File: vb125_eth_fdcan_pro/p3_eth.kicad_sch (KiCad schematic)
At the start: 28 parts, among them U2 LAN8740A, X1 50MHz

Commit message: vb125: H7 schematic WIP.
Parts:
- removed R11, R12, R13: 33R, symbol Device:R_Small
- added R11, R12, R13: 33R, Resistor_SMD:R_0402_1005Metric, symbol Device:R
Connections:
- net ETH_CRS_DV: now also R11.1
- net ETH_RXD0: now also R12.1
- net ETH_RXD1: now also R13.1
- net RXD0: now also R12.2
- net RXD1: now also R13.2
- net at R8.2, U2.15 (COL/CRS_DV/MODE2): now also R11.2
- no-connect marks 1 -> 4

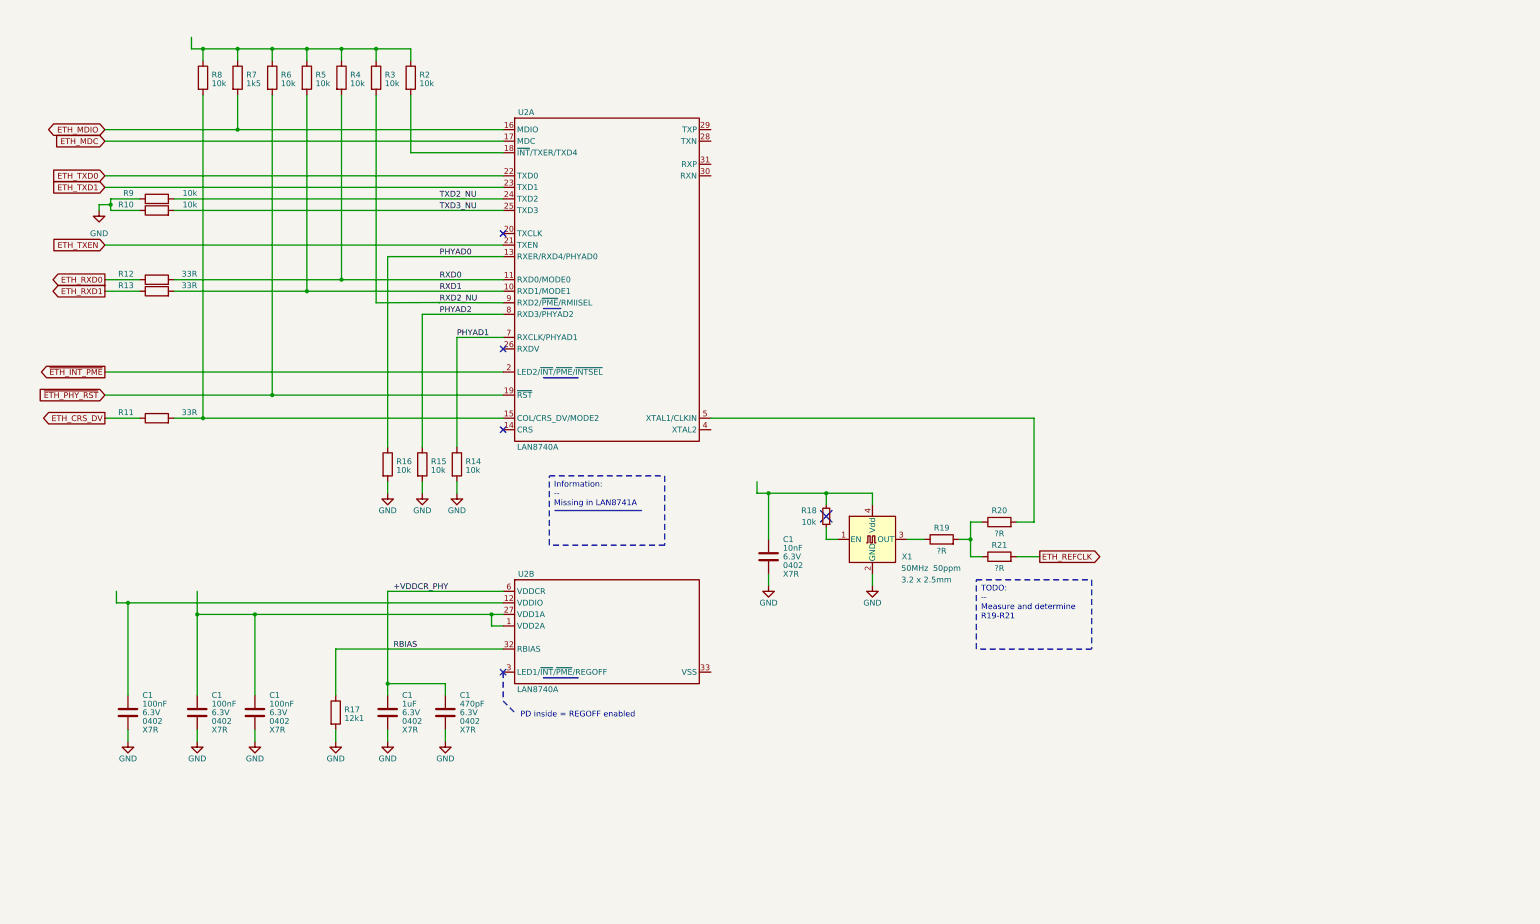
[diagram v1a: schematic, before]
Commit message: AOZ schematic. 3V3 DC-DC. Partly bus power.
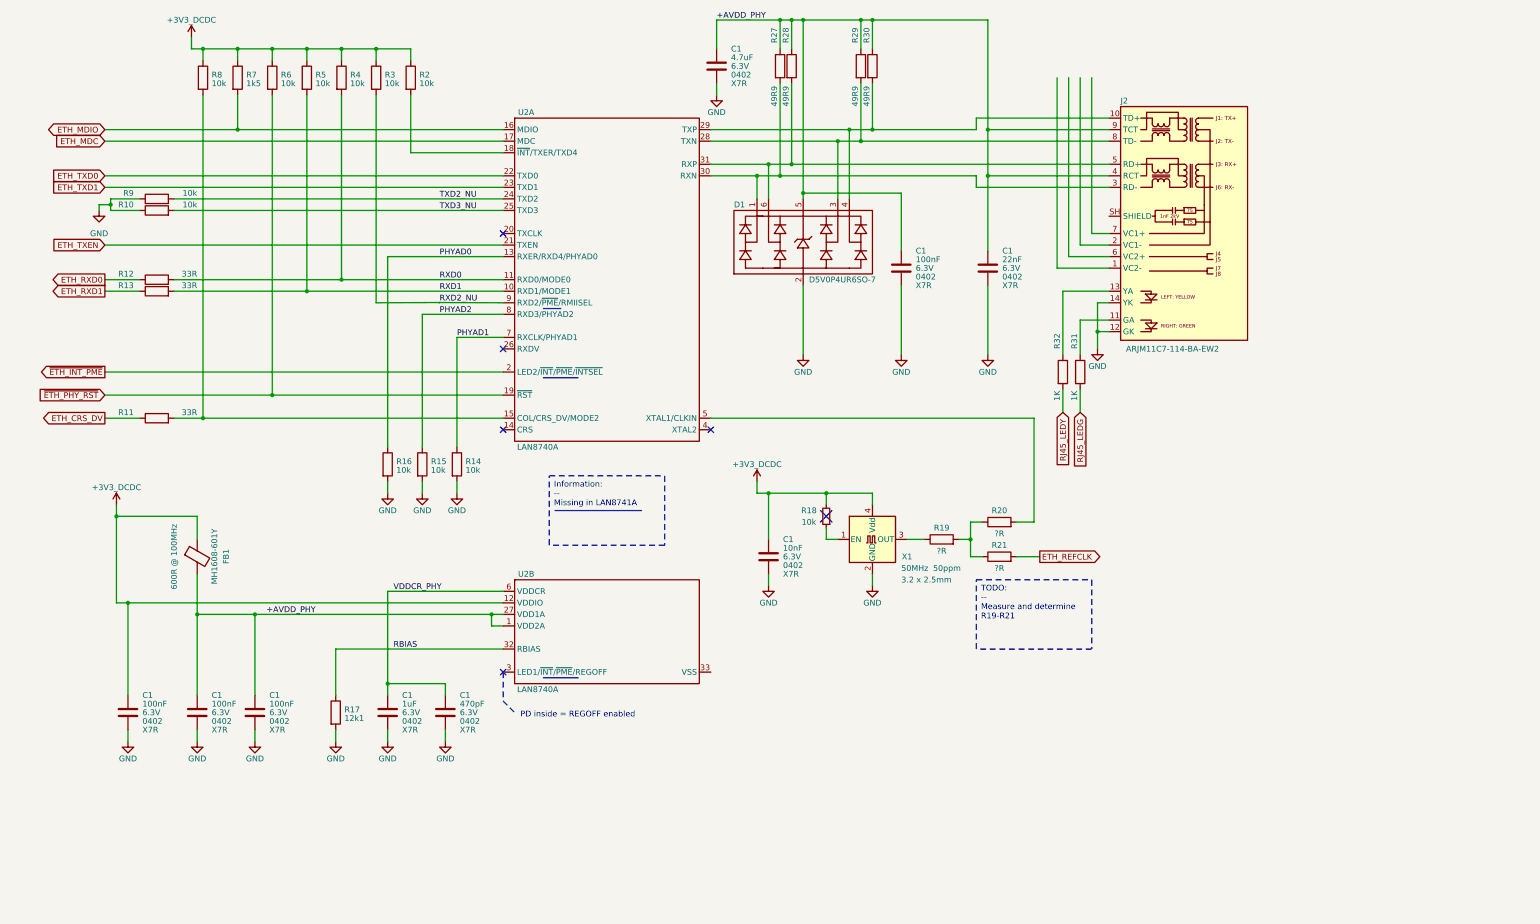
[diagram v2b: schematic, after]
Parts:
- added C1: 22nF, symbol Device:C
- added C1: 100nF, symbol Device:C
- added C1: 4.7uF, symbol Device:C
- added D1: D5V0P4UR6SO-7, vhrd_passive_tvs:D5V0P4UR6SO-7, symbol vhrd_passive_tvs:D5V0P4UR6SO-7
- added FB1: MH1608-601Y, symbol Device:FerriteBead
- added J2: ARJM11C7-114-BA-EW2, vhrd_connector_abracon:RJ45_Abracon_ARJM11_7POE_LED, symbol vhrd_connector_abracon:ARJM11C7-114-BA
- added R27, R28, R29, R30: 49R9, Resistor_SMD:R_0402_1005Metric, symbol Device:R
- added R31, R32: 1K, Resistor_SMD:R_0402_1005Metric, symbol Device:R
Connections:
- net GND: now also C1.2, C1.2, C1.2, D1.2 (VSS), J2.12 (GK), J2.14 (YK)
- net at U2.28 (TXN): now also D1.3 (I/O_2), J2.8 (TD-), R29.2
- net at U2.29 (TXP): now also D1.4 (I/O_3), J2.10 (TD+), R30.2
- net at U2.30 (RXN): now also D1.1 (I/O_1), J2.3 (RD-), R27.2
- net at U2.31 (RXP): now also D1.6 (I/O_4), J2.5 (RD+), R28.2
- net +3V3_DCDC: now reaches R2.1, R3.1, R4.1, R5.1, R6.1, R7.1, R8.1
- net +3V3_DCDC: now also C1.1, C1.1, R18.2, U2.12 (VDDIO), X1.4 (Vdd), FB1.1
- net +AVDD_PHY: now reaches C1.1, C1.1, U2.1 (VDD2A), U2.27 (VDD1A)
- net +AVDD_PHY: now also C1.1, C1.1, C1.1, D1.5 (VCC), FB1.2, J2.4 (RCT), J2.9 (TCT), R27.1, R28.1, R29.1, R30.1
- net +VDDCR_PHY renamed VDDCR_PHY
- new net: J2.13 (YA), R32.1
- new net: J2.11 (GA), R31.1
- new net RJ45_LEDG: R31.2
- new net RJ45_LEDY: R32.2
- no-connect marks 4 -> 5

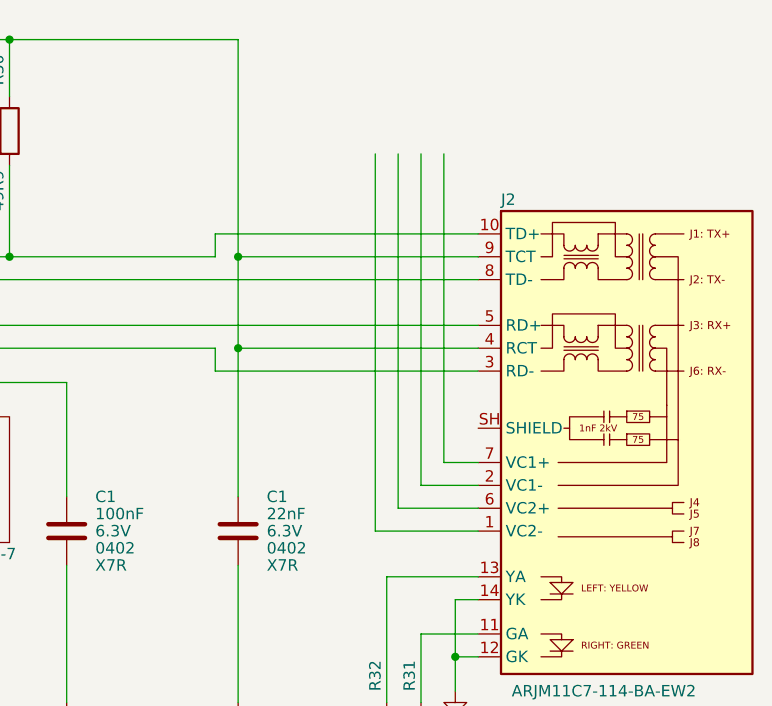
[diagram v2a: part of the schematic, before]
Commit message: Work on PoE. Rearrange pages.
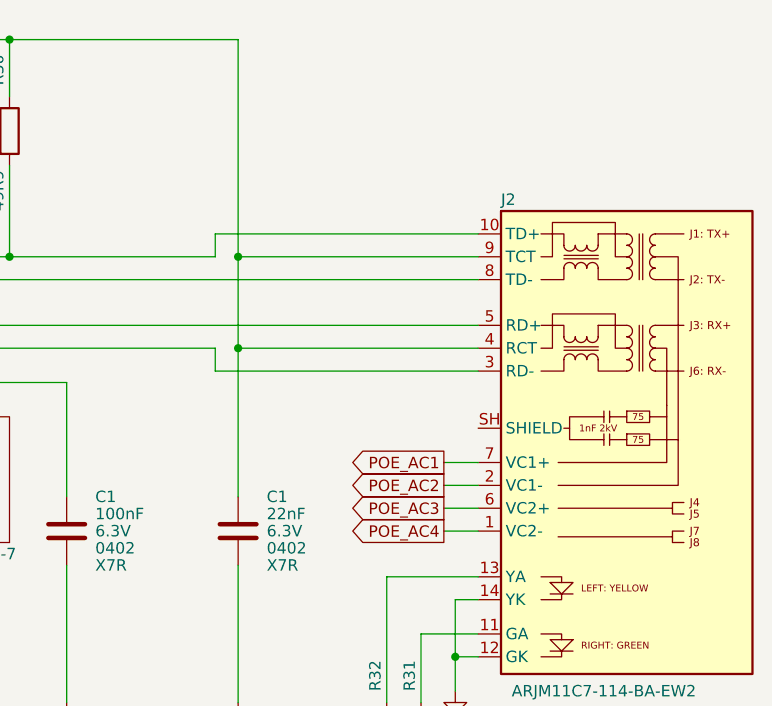
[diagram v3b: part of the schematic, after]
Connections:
- net POE_AC4: now reaches J2.1 (VC2-)
- net POE_AC2: now reaches J2.2 (VC1-)
- net POE_AC3: now reaches J2.6 (VC2+)
- net POE_AC1: now reaches J2.7 (VC1+)
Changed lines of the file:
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@@
-    (stroke (width 0) (type default))
-  )
-  (wire (pts (xy 243.84 38.1) (xy 243.84 74.93))
     (stroke (width 0) (type default))
   )
@@
     (stroke (width 0) (type default))
   )
-  (wire (pts (xy 246.38 38.1) (xy 246.38 72.39))
-    (stroke (width 0) (type default))
-  )
   (wire (pts (xy 190.5 52.07) (xy 195.58 52.07))
     (stroke (width 0) (type default))
@@
     (stroke (width 0) (type default) (color 194 0 0 1))
   )
-  (wire (pts (xy 241.3 38.1) (xy 241.3 77.47))
-    (stroke (width 0) (type default))
-  )
   (wire (pts (xy 180.34 39.37) (xy 180.34 57.15))
     (stroke (width 0) (type default))
@@
     (stroke (width 0.254) (type default) (color 194 0 0 1))
   )
+  (wire (pts (xy 250.19 77.47) (xy 246.38 77.47))
+    (stroke (width 0) (type default))
+  )
   (wire (pts (xy 104.14 173.99) (xy 104.14 171.45))
     (stroke (width 0) (type default))
@@
   )
   (wire (pts (xy 91.44 127) (xy 91.44 129.54))
+    (stroke (width 0) (type default))
+  )
+  (wire (pts (xy 250.19 74.93) (xy 246.38 74.93))
     (stroke (width 0) (type default))
   )
@@
     (stroke (width 0) (type default))
   )
-  (wire (pts (xy 250.19 80.01) (xy 238.76 80.01))
-    (stroke (width 0) (type default))
-  )
   (wire (pts (xy 223.52 59.69) (xy 223.52 76.2))
     (stroke (width 0) (type default))
@@
     (stroke (width 0) (type default))
   )
+  (wire (pts (xy 250.19 80.01) (xy 246.38 80.01))
+    (stroke (width 0) (type default))
+  )
   (wire (pts (xy 223.52 83.82) (xy 223.52 99.06))
     (stroke (width 0) (type default))
@@
   )
   (wire (pts (xy 88.9 31.75) (xy 96.52 31.75))
-    (stroke (width 0) (type default))
-  )
-  (wire (pts (xy 250.19 74.93) (xy 243.84 74.93))
     (stroke (width 0) (type default))
   )
@@
     (stroke (width 0) (type default))
   )
-  (wire (pts (xy 250.19 77.47) (xy 241.3 77.47))
-    (stroke (width 0) (type default))
-  )
   (wire (pts (xy 30.48 67.31) (xy 36.83 67.31))
     (stroke (width 0) (type default))
@@
   )
   (wire (pts (xy 34.29 153.67) (xy 116.84 153.67))
-    (stroke (width 0) (type default))
-  )
-  (wire (pts (xy 238.76 38.1) (xy 238.76 80.01))
     (stroke (width 0) (type default))
   )
@@
     )
   )
+  (global_label "POE_AC1" (shape output) (at 246.38 72.39 180) (fields_autoplaced)
+    (effects (font (size 1.27 1.27)) (justify right))
+    (property "Intersheetrefs" "${INTERSHEET_REFS}" (at 235.189 72.39 0)
+      (effects (font (size 1.27 1.27)) (justify right) hide)
+    )
+  )
+  (global_label "POE_AC4" (shape output) (at 246.38 80.01 180) (fields_autoplaced)
+    (effects (font (size 1.27 1.27)) (justify right))
+    (property "Intersheetrefs" "${INTERSHEET_REFS}" (at 235.189 80.01 0)
+      (effects (font (size 1.27 1.27)) (justify right) hide)
+    )
+  )
   (global_label "~{ETH_PHY_RST}" (shape input) (at 29.21 107.95 180) (fields_autoplaced)
     (effects (font (size 1.27 1.27)) (justify right))
@@
     )
   )
+  (global_label "POE_AC2" (shape output) (at 246.38 74.93 180) (fields_autoplaced)
+    (effects (font (size 1.27 1.27)) (justify right))
+    (property "Intersheetrefs" "${INTERSHEET_REFS}" (at 235.189 74.93 0)
+      (effects (font (size 1.27 1.27)) (justify right) hide)
+    )
+  )
   (global_label "~{ETH_INT_PME}" (shape output) (at 29.21 102.87 180) (fields_autoplaced)
     (effects (font (size 1.27 1.27)) (justify right))
@@
       (effects (font (size 1.27 1.27)) (justify right) hide)
     )
+  )
+  (global_label "POE_AC3" (shape output) (at 246.38 77.47 180) (fields_autoplaced)
+    (effects (font (size 1.27 1.27)) (justify right))
+    (property "Intersheetrefs" "${INTERSHEET_REFS}" (at 235.189 77.47 0)
+      (effects (font (size 1.27 1.27)) (justify right) hide)
+    )

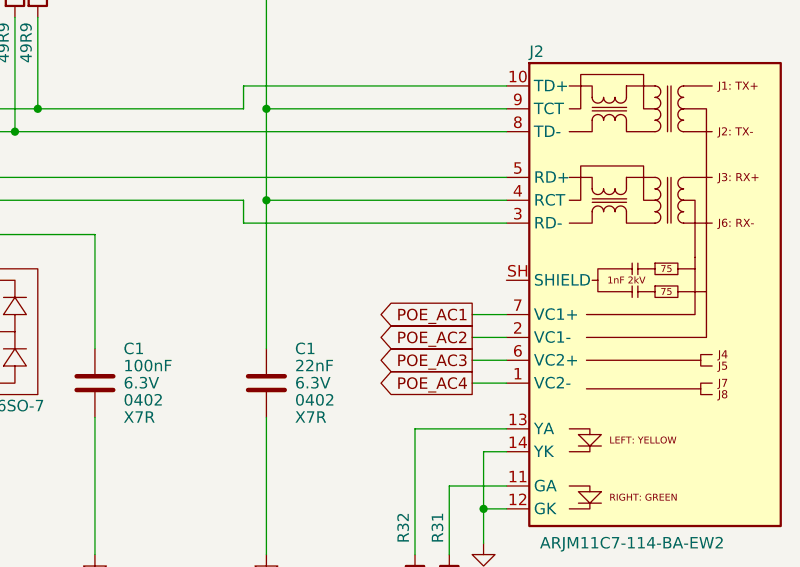
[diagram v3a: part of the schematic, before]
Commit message: CAN schematics. Assign IO on H7.
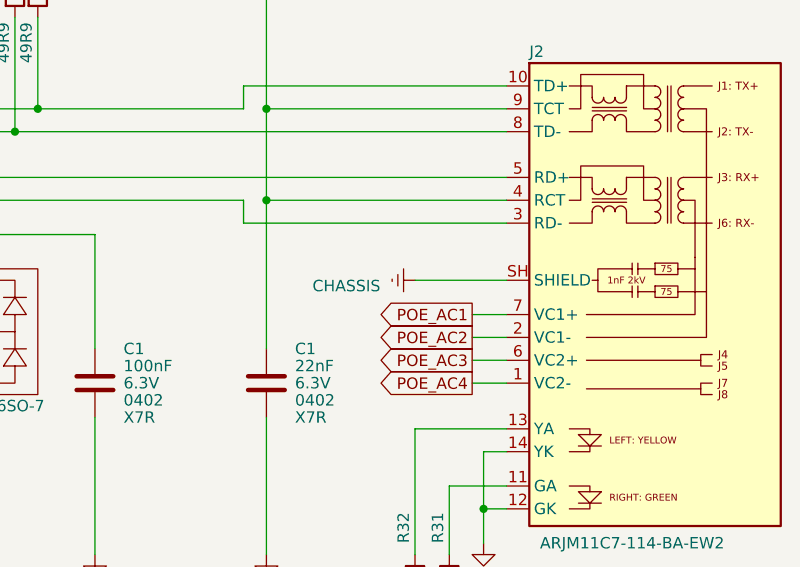
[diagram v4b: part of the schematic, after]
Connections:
- net CHASSIS: now reaches J2.SH (SHIELD)
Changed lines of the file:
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@@
+    (stroke (width 0) (type default))
+  )
+  (wire (pts (xy 240.03 68.58) (xy 250.19 68.58))
     (stroke (width 0) (type default))
   )
@@
         )
       )
+    )
+  )
+  (symbol (lib_id "vhrd_power:CHASSIS") (at 240.03 68.58 270) (unit 1)
+    (in_bom yes) (on_board yes) (dnp no) (fields_autoplaced)
+    (property "Reference" "#PWR0153" (at 233.68 68.58 0)
+      (effects (font (size 1.27 1.27)) hide)
+    )
+    (property "Value" "CHASSIS" (at 232.41 69.215 90)
+      (effects (font (size 1.27 1.27)))
+    )
+    (property "Footprint" "" (at 240.03 68.58 0)
+      (effects (font (size 1.27 1.27)) hide)
+    )
+    (property "Datasheet" "~" (at 240.03 68.58 0)
+      (effects (font (size 1.27 1.27)) hide)
+    )
+    (pin "1")
+    (instances
+      (project "vb125_eth_fdcan_pro"
+        (path "/b473bccb-f14c-41d5-b473-137d3ef8ae1e/13d04be1-6d05-4847-9c03-a8fbeeb3fd19"
+          (reference "#PWR0153") (unit 1)
+        )
+        (path "/b473bccb-f14c-41d5-b473-137d3ef8ae1e/6eaf8f36-f4c1-413f-846c-b502b7be2b8c"
+          (reference "#PWR0154") (unit 1)
+        )
+      )

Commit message: Finish schematics.
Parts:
- C1: footprint (none) -> Capacitor_SMD:C_0402_1005Metric
- FB1: footprint (none) -> Inductor_SMD:L_0603_1608Metric
- R18: footprint (none) -> Resistor_SMD:R_0402_1005Metric
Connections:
- net GND: now also U2.33 (VSS)
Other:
- note added: "50MHz REFCLK"
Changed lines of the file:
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@@
-    (stroke (width 0) (type default))
-  )
-  (wire (pts (xy 102.6427 87.5756) (xy 88.9 87.63))
     (stroke (width 0) (type default))
   )
@@
     (stroke (width 0) (type default))
   )
-  (wire (pts (xy 102.87 87.5756) (xy 102.6427 87.5756))
-    (stroke (width 0) (type default))
-  )
   (wire (pts (xy 240.03 99.06) (xy 240.03 85.09))
     (stroke (width 0) (type default))
@@
   )
   (wire (pts (xy 243.84 91.44) (xy 250.19 91.44))
+    (stroke (width 0) (type default))
+  )
+  (wire (pts (xy 165.1 168.91) (xy 162.56 168.91))
     (stroke (width 0) (type default))
   )
@@
     (stroke (width 0) (type default))
   )
+  (wire (pts (xy 165.1 184.15) (xy 165.1 168.91))
+    (stroke (width 0) (type default))
+  )
   (wire (pts (xy 88.9 31.75) (xy 96.52 31.75))
     (stroke (width 0) (type default))
@@
   )
   (wire (pts (xy 220.98 46.99) (xy 250.19 46.99))
+    (stroke (width 0) (type default))
+  )
+  (wire (pts (xy 88.9 87.63) (xy 116.84 87.63))
     (stroke (width 0) (type default))
   )
@@
     (stroke (width 0.254) (type default) (color 194 0 0 1))
   )
-  (wire (pts (xy 116.84 87.63) (xy 102.6427 87.5756))
-    (stroke (width 0) (type default))
-  )
   (wire (pts (xy 81.28 31.75) (xy 88.9 31.75))
     (stroke (width 0) (type default))
@@
   )
   (wire (pts (xy 195.58 25.4) (xy 195.58 31.75))
-    (stroke (width 0) (type default))
-  )
-  (wire (pts (xy 102.87 87.63) (xy 102.87 87.5756))
     (stroke (width 0) (type default))
   )
@@
     (effects (font (size 1.27 1.27)) (justify left top))
   )
+  (text "50MHz REFCLK" (at 185.42 124.46 0)
+    (effects (font (size 2.54 2.54)) (justify left bottom))
+  )
   (text "PD inside = REGOFF enabled " (at 120.65 179.07 0)
     (effects (font (size 1.27 1.27)) (justify left bottom))
@@
       (effects (font (size 1.27 1.27)) (justify left))
     )
-    (property "Footprint" "" (at 224.4852 83.82 0)
+    (property "Footprint" "Capacitor_SMD:C_0402_1005Metric" (at 224.4852 83.82 0)
       (effects (font (size 1.27 1.27)) hide)
     )
@@
       (effects (font (size 1.27 1.27)))
     )
-    (property "Footprint" "" (at 47.752 143.51 90)
+    (property "Footprint" "Inductor_SMD:L_0603_1608Metric" (at 47.752 143.51 90)
       (effects (font (size 1.27 1.27)) hide)
     )
@@
       (effects (font (size 1.27 1.27)) (justify left))
     )
-    (property "Footprint" "" (at 205.4352 83.82 0)
+    (property "Footprint" "Capacitor_SMD:C_0402_1005Metric" (at 205.4352 83.82 0)
       (effects (font (size 1.27 1.27)) hide)
     )
@@
       (effects (font (size 1.27 1.27)) (justify left))
     )
-    (property "Footprint" "" (at 92.4052 181.61 0)
+    (property "Footprint" "Capacitor_SMD:C_0402_1005Metric" (at 92.4052 181.61 0)
       (effects (font (size 1.27 1.27)) hide)
     )
@@
       (effects (font (size 1.27 1.27)) (justify left))
     )
-    (property "Footprint" "" (at 63.1952 181.61 0)
+    (property "Footprint" "Capacitor_SMD:C_0402_1005Metric" (at 63.1952 181.61 0)
       (effects (font (size 1.27 1.27)) hide)
     )
@@
     )
   )
+  (symbol (lib_id "power:GND") (at 165.1 184.15 0) (unit 1)
+    (in_bom yes) (on_board yes) (dnp no)
+    (property "Reference" "#PWR0157" (at 165.1 190.5 0)
+      (effects (font (size 1.27 1.27)) hide)
+    )
+    (property "Value" "GND" (at 165.1 187.96 0)
+      (effects (font (size 1.27 1.27)))
+    )
+    (property "Footprint" "" (at 165.1 184.15 0)
+      (effects (font (size 1.27 1.27)) hide)
+    )
+    (property "Datasheet" "" (at 165.1 184.15 0)
+      (effects (font (size 1.27 1.27)) hide)
+    )
+    (pin "1")
+    (instances
+      (project "vb125_eth_fdcan_pro"
+        (path "/b473bccb-f14c-41d5-b473-137d3ef8ae1e/6eaf8f36-f4c1-413f-846c-b502b7be2b8c"
+          (reference "#PWR0157") (unit 1)
+        )
+      )
+    )
+  )
   (symbol (lib_id "Device:C") (at 49.53 177.8 0) (unit 1)
     (in_bom yes) (on_board yes) (dnp no)
@@
       (effects (font (size 1.27 1.27)) (justify left))
     )
-    (property "Footprint" "" (at 50.4952 181.61 0)
+    (property "Footprint" "Capacitor_SMD:C_0402_1005Metric" (at 50.4952 181.61 0)
       (effects (font (size 1.27 1.27)) hide)
     )
@@
       (effects (font (size 1.27 1.27)) (justify left))
     )
-    (property "Footprint" "" (at 105.1052 181.61 0)
+    (property "Footprint" "Capacitor_SMD:C_0402_1005Metric" (at 105.1052 181.61 0)
       (effects (font (size 1.27 1.27)) hide)
     )
@@
       (effects (font (size 1.27 1.27)) (justify left))
     )
-    (property "Footprint" "" (at 35.2552 181.61 0)
+    (property "Footprint" "Capacitor_SMD:C_0402_1005Metric" (at 35.2552 181.61 0)
       (effects (font (size 1.27 1.27)) hide)
     )
@@
       (effects (font (size 1.27 1.27)) (justify left))
     )
-    (property "Footprint" "" (at 176.2252 147.32 0)
+    (property "Footprint" "Capacitor_SMD:C_0402_1005Metric" (at 176.2252 147.32 0)
       (effects (font (size 1.27 1.27)) hide)
     )
@@
       (effects (font (size 1.27 1.27)) (justify left))
     )
-    (property "Footprint" "" (at 164.7952 39.37 0)
+    (property "Footprint" "Capacitor_SMD:C_0402_1005Metric" (at 164.7952 39.37 0)
       (effects (font (size 1.27 1.27)) hide)
     )
@@
       (effects (font (size 1.27 1.27)))
     )
-    (property "Footprint" "" (at 187.96 134.62 0)
-      (effects (font (size 1.27 1.27)) hide)
-    )
+    (property "Footprint" "Resistor_SMD:R_0402_1005Metric" (at 187.96 134.62 0)
+      (effects (font (size 1.27 1.27)) hide)
+    )
